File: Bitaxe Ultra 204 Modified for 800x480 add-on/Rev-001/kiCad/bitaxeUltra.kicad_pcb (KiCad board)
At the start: 4 copper layers, 56.5 x 99.8 mm, 146 parts, among them J1 54-00164, J10 Conn_01x02, J2 Conn_01x02, J3 Conn_01x05, J4 Conn_01x04, J5 TC2030-IDC, J6 Conn_01x04, J7 Conn_01x02, J8 USB_C_Receptacle_USB2.0, J9 Conn_01x04, Q1 CSD17311Q5, Q2 CSD17311Q5, Q4 2N7002K, SW1 GT-TC029B-H025-L1N, SW2 GT-TC029B-H025-L1N, U1 25MHz, U10 DS4432U+, U11 RT9080-33GJ5, U12 ESP32-S3-WROOM-1, U14 BM1366_mode1, U2 TXB0104RGYR, U5 MCP1824T-1802E, U6 MCP1824T-0802E, U7 EMC2101, U8 INA260, U9 TPS40305, Y1 32.768kHz

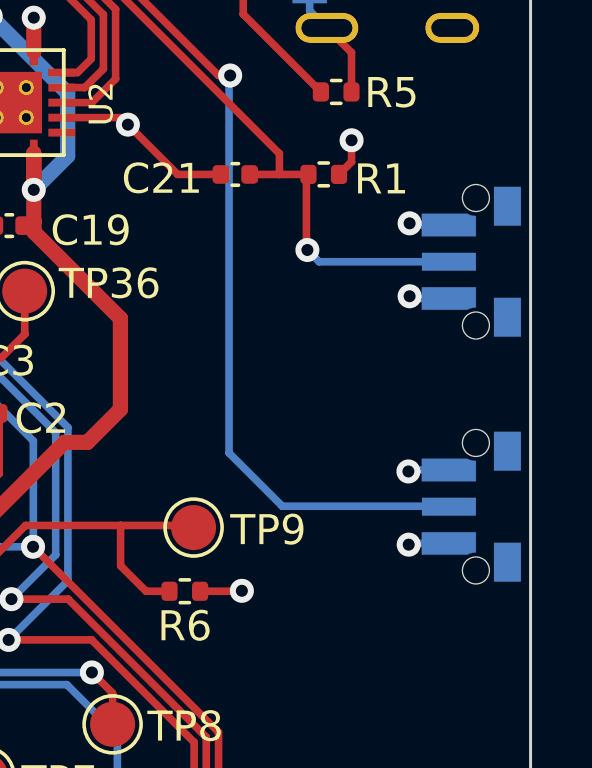
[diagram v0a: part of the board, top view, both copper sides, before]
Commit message: added solder points to hold down reset button
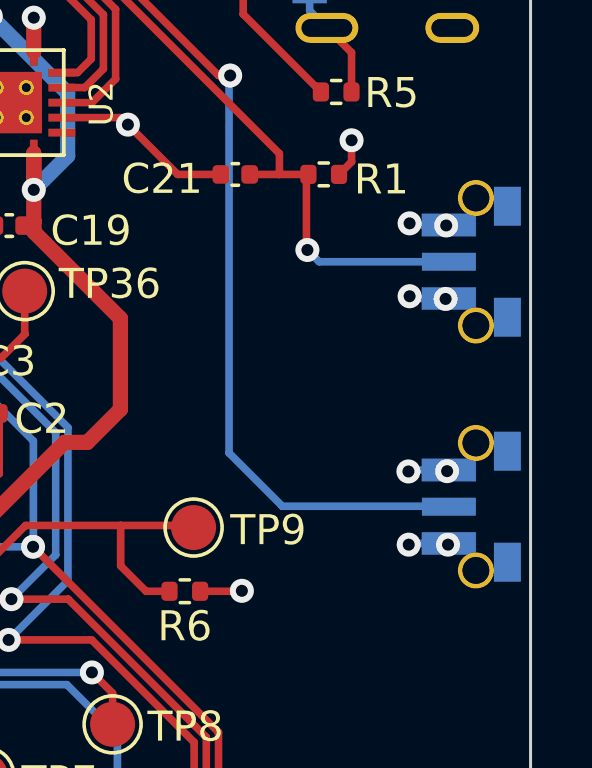
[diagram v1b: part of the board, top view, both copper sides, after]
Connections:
- SW1 pad : (no net) -> GND
- SW2 pad : (no net) -> GND
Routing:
- net GND: track 146.1 -> 146.2 mm, vias 85 -> 89
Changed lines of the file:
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@@
 			(layer "B.Fab")
 		)
-		(pad "" np_thru_hole circle
+		(pad "" thru_hole circle
 			(at -2.125 0 270)
-			(size 0.9 0.9)
+			(size 1.2 1.2)
 			(drill 0.9)
 			(layers "*.Cu" "*.Mask")
+			(remove_unused_layers no)
+			(net 1 "GND")
 		)
-		(pad "" np_thru_hole circle
+		(pad "" thru_hole circle
 			(at 2.125 0 270)
-			(size 0.9 0.9)
+			(size 1.2 1.2)
 			(drill 0.9)
 			(layers "*.Cu" "*.Mask")
+			(remove_unused_layers no)
+			(net 1 "GND")
 		)
 		(pad "1" smd custom
@@
 			(layer "B.Fab")
 		)
-		(pad "" np_thru_hole circle
+		(pad "" thru_hole circle
 			(at -2.125 0 270)
-			(size 0.9 0.9)
+			(size 1.2 1.2)
 			(drill 0.9)
 			(layers "*.Cu" "*.Mask")
+			(remove_unused_layers no)
+			(net 1 "GND")
 		)
-		(pad "" np_thru_hole circle
+		(pad "" thru_hole circle
 			(at 2.125 0 270)
-			(size 0.9 0.9)
+			(size 1.2 1.2)
 			(drill 0.9)
 			(layers "*.Cu" "*.Mask")
+			(remove_unused_layers no)
+			(net 1 "GND")
 		)
 		(pad "1" smd custom
@@
 	)
 	(via
+		(at 130.9 105.81)
+		(size 0.8)
+		(drill 0.4)
+		(layers "F.Cu" "B.Cu")
+		(net 1)
+	)
+	(via
 		(at 101.092 98.552)
 		(size 0.8)
@@
 	)
 	(via
+		(at 130.98 114)
+		(size 0.8)
+		(drill 0.4)
+		(layers "F.Cu" "B.Cu")
+		(net 1)
+	)
+	(via
 		(at 105.673 117.442)
 		(size 0.8)
@@
 	)
 	(via
+		(at 130.92 103.36)
+		(size 0.8)
+		(drill 0.4)
+		(layers "F.Cu" "B.Cu")
+		(net 1)
+	)
+	(via
 		(at 101.092 97.536)
 		(size 0.8)
@@
 	)
 	(via
+		(at 130.95 111.55)
+		(size 0.8)
+		(drill 0.4)
+		(layers "F.Cu" "B.Cu")
+		(net 1)
+	)
+	(via
 		(at 104.43 130.24)
 		(size 0.8)
@@
 	(segment
 		(start 131.15 105.795)
-		(end 129.775 105.795)
+		(end 130.915 105.795)
 		(width 0.254)
 		(layer "B.Cu")
@@
 	)
 	(segment
+		(start 130.885 105.795)
+		(end 129.775 105.795)
+		(width 0.254)
+		(layer "B.Cu")
+		(net 1)
+	)
+	(segment
 		(start 99.4012 114.311)
 		(end 97.2142 112.124)
@@
 	)
 	(segment
+		(start 130.915 105.795)
+		(end 130.9 105.81)
+		(width 0.254)
+		(layer "B.Cu")
+		(net 1)
+	)
+	(segment
+		(start 130.95 111.55)
+		(end 130.91 111.51)
+		(width 0.254)
+		(layer "B.Cu")
+		(net 1)
+	)
+	(segment
 		(start 125.6 65.94)
 		(end 125.6 63.95)
@@
 	)
 	(segment
+		(start 130.905 103.345)
+		(end 129.755 103.345)
+		(width 0.254)
+		(layer "B.Cu")
+		(net 1)
+	)
+	(segment
+		(start 130.935 103.345)
+		(end 130.92 103.36)
+		(width 0.254)
+		(layer "B.Cu")
+		(net 1)
+	)
+	(segment
+		(start 131.02 113.96)
+		(end 131.265 113.96)
+		(width 0.254)
+		(layer "B.Cu")
+		(net 1)
+	)
+	(segment
 		(start 110.862 119.033)
 		(end 110.156 118.327)
@@
 	)
 	(segment
+		(start 130.94 113.96)
+		(end 130.98 114)
+		(width 0.254)
+		(layer "B.Cu")
+		(net 1)
+	)
+	(segment
 		(start 129.71 113.96)
-		(end 131.265 113.96)
+		(end 130.94 113.96)
 		(width 0.254)
 		(layer "B.Cu")
@@
 	(segment
 		(start 131.265 111.51)
-		(end 129.71 111.51)
+		(end 130.99 111.51)
+		(width 0.254)
+		(layer "B.Cu")
+		(net 1)
+	)
+	(segment
+		(start 130.9 105.81)
+		(end 130.885 105.795)
 		(width 0.254)
 		(layer "B.Cu")
@@
 	)
 	(segment
+		(start 130.99 111.51)
+		(end 130.95 111.55)
+		(width 0.254)
+		(layer "B.Cu")
+		(net 1)
+	)
+	(segment
+		(start 130.91 111.51)
+		(end 129.71 111.51)
+		(width 0.254)
+		(layer "B.Cu")
+		(net 1)
+	)
+	(segment
 		(start 99.393 122.727)
 		(end 99.393 119.299)
@@
 	)
 	(segment
+		(start 130.92 103.36)
+		(end 130.905 103.345)
+		(width 0.254)
+		(layer "B.Cu")
+		(net 1)
+	)
+	(segment
 		(start 100.374 118.318)
 		(end 102.696 118.318)
@@
 	)
 	(segment
+		(start 130.98 114)
+		(end 131.02 113.96)
+		(width 0.254)
+		(layer "B.Cu")
+		(net 1)
+	)
+	(segment
 		(start 97.2142 112.124)
 		(end 96.109 112.124)
@@
 	(segment
 		(start 131.15 103.345)
-		(end 129.755 103.345)
+		(end 130.935 103.345)
 		(width 0.254)
 		(layer "B.Cu")
